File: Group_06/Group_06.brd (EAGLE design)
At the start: 100 x 80 mm, 29 parts, among them J1 POWER_JACKPTH_LOCK, U2 +12v

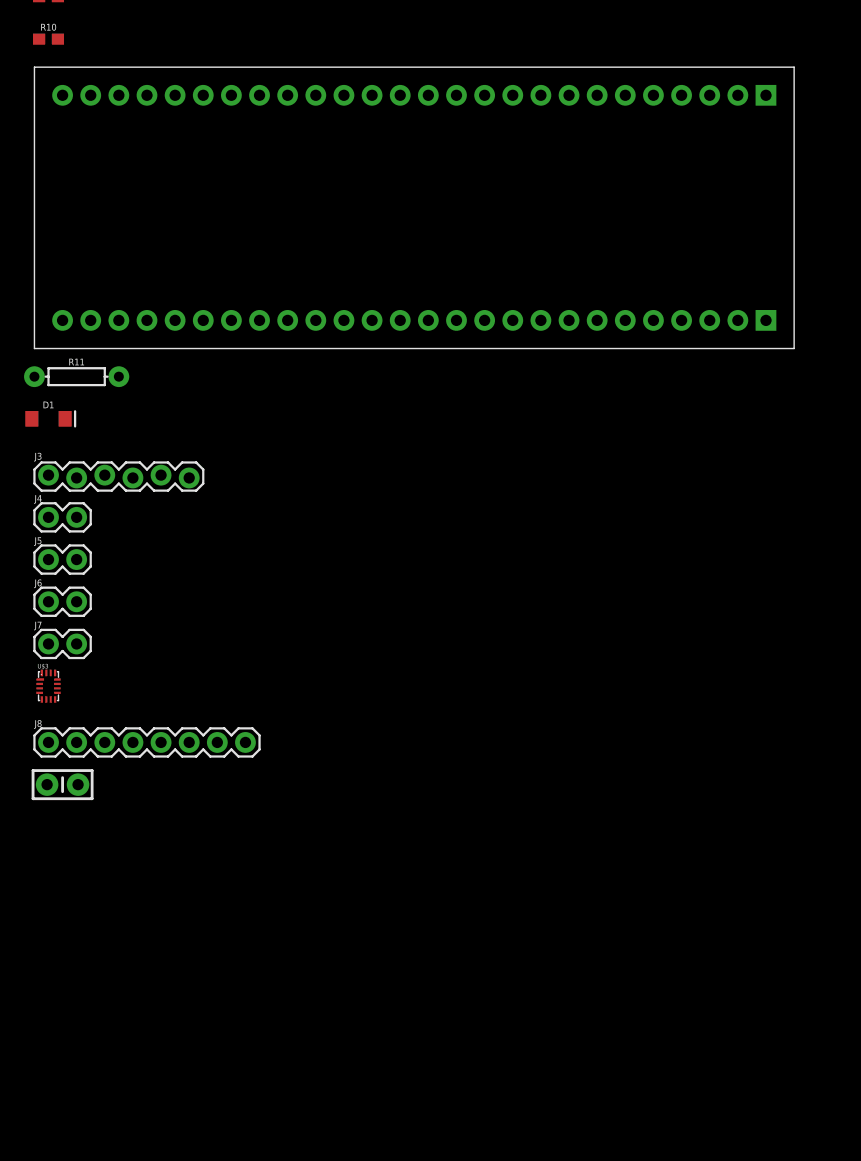
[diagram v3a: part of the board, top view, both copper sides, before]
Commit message: Change microcontroller and fixing connection problem
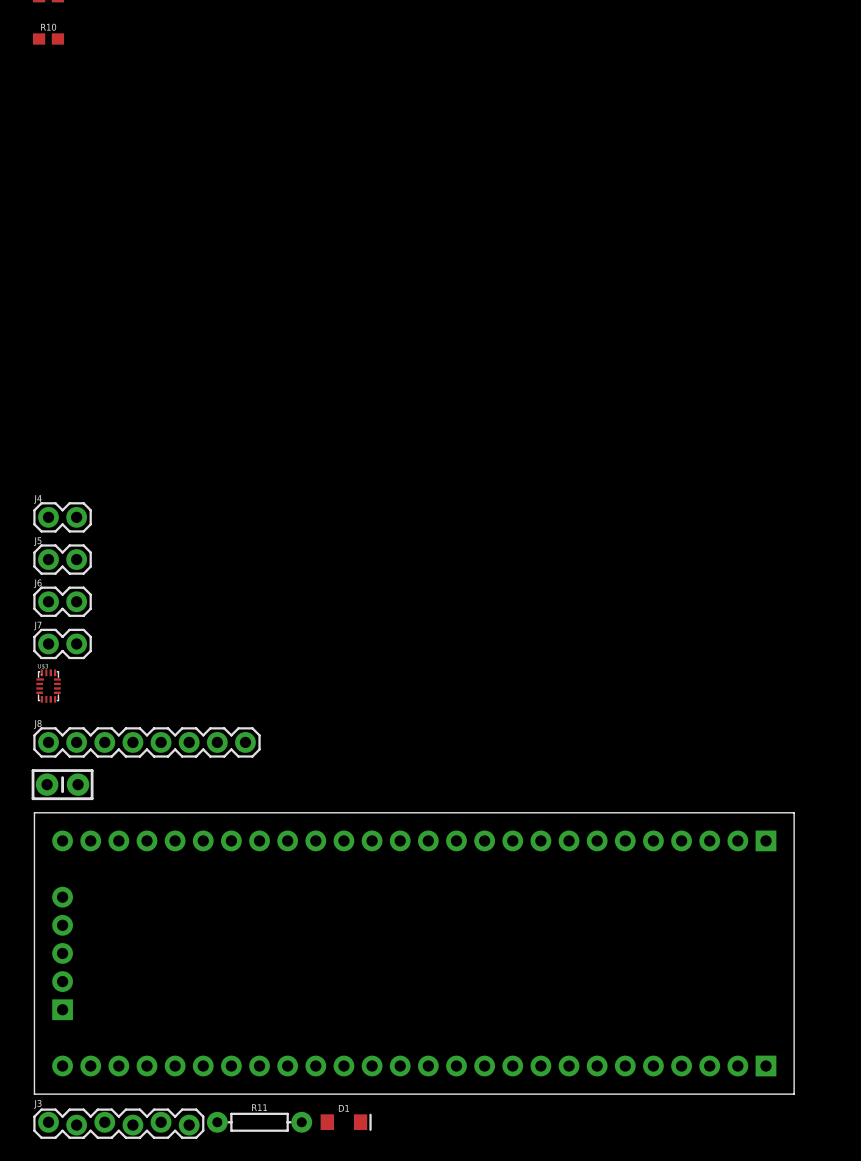
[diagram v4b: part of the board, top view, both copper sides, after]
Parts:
- U$2: value CY8CKIT-059_TARGET_3 -> CY8CKIT-059_TARGET; device CY8KIT-059:CY8CKIT-059_TARGET_3 -> CY8KIT-059:CY8CKIT-059_TARGET
- moved R11 69.3 mm to (-31.8, -143.5)
- moved D1 68.9 mm to (-24.1, -143.5)
- moved U$2 67.3 mm to (-16.5, -127.0)
- moved J3 58.4 mm to (-50.8, -143.5)
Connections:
- removed net GND2: U$2.52
- removed net MUX_A0/1.3C: U$3.15
- removed net MUX_A0/2.3C: U$2.24
- removed net MUX_A1/2.3C: U$2.23
- removed net MUX_A2/2.3C: U$2.22
- removed net MUX_OUT/2.5C: U$2.21
- removed net N$19: U$3.14
- removed net N$20: U$3.13
- removed net N$23: U$3.6
- new net MUX_A0: U$2.24, U$3.15
- new net MUX_A1: U$2.23, U$3.14
- new net MUX_A2: U$2.22, U$3.13
- new net MUX_OUT: U$2.21, U$3.6

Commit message: first try board
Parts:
- moved C3 226.3 mm to (95.2, 61.0), turned to 90 degrees
- moved J8 224.7 mm to (72.4, 78.7), turned to 180 degrees
- moved U$3 192.0 mm to (53.3, 57.1)
- moved J3 180.1 mm to (54.6, 2.54), turned to 180 degrees
- moved U$2 172.3 mm to (36.8, 36.8)
- moved J4 168.7 mm to (2.54, 71.1), turned to 90 degrees
- moved J5 166.3 mm to (2.54, 64.8), turned to 90 degrees
- moved J6 163.9 mm to (2.54, 58.4), turned to 90 degrees
- moved J7 161.5 mm to (2.54, 52.1), turned to 90 degrees
- moved R11 155.1 mm to (20.3, 2.54), turned to 180 degrees
- moved D1 149.5 mm to (7.62, 2.54)
- moved S1 148.0 mm to (80.0, 77.5), turned to 270 degrees
- moved U2 146.9 mm to (90.2, 73.7)
- moved C2 128.9 mm to (82.5, 61.0), turned to 90 degrees
- moved R10 119.4 mm to (14.0, 54.6), turned to 270 degrees
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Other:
- board size 100 x 80 mm -> 97.8 x 83.8 mm

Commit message: Board Layout 1
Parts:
- moved S1 72.0 mm to (55.0, 9.91), turned to 0 degrees
- moved U2 63.8 mm to (62.9, 16.0)
- moved C3 62.1 mm to (62.7, 8.00), turned to 180 degrees
- moved C2 60.0 mm to (62.7, 4.32), turned to 180 degrees
- moved J7 57.3 mm to (58.4, 64.8), turned to 180 degrees
- moved J1 55.9 mm to (47.6, 18.5), turned to 180 degrees
- moved J8 52.7 mm to (21.6, 64.8)
- moved J6 47.4 mm to (49.5, 64.8), turned to 180 degrees
- moved R10 44.9 mm to (58.4, 61.0)
- moved R9 44.9 mm to (55.9, 61.0)
- moved R8 43.6 mm to (49.5, 61.0)
- moved U$3 40.7 mm to (12.7, 55.9)
- moved J2 40.6 mm to (69.8, 7.62)
- moved R7 38.6 mm to (47.0, 61.0)
- moved J4 36.1 mm to (38.1, 64.8), turned to 0 degrees
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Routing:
- added copper zone on layer 16, net 5V
- added copper zone on layer 1, net GND
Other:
- board size 97.8 x 83.8 mm -> 72.4 x 69.8 mm

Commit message: Board Layout 2
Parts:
- moved J2 45.7 mm to (68.6, 53.3)
- moved J4 27.9 mm to (66.0, 64.8), turned to 180 degrees
- moved R4 27.9 mm to (66.0, 61.0)
- moved J7 26.7 mm to (31.8, 64.8)
- moved R10 26.7 mm to (31.8, 61.0)
- moved R9 26.7 mm to (29.2, 61.0)
- moved J5 26.7 mm to (54.6, 64.8), turned to 180 degrees
- moved R6 26.7 mm to (54.6, 61.0)
- moved R3 22.9 mm to (63.5, 61.0)
- moved R5 21.6 mm to (52.1, 61.0)
- moved R2 19.4 mm to (10.2, 20.8), turned to 0 degrees
- moved U2 19.2 mm to (43.7, 16.8), turned to 90 degrees
- moved C2 14.0 mm to (48.8, 5.59)
- moved C3 14.0 mm to (48.8, 9.27)
- moved S1 12.9 mm to (63.8, 19.4), turned to 90 degrees
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
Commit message: Board Layout 3
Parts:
- moved C3 27.1 mm to (22.1, 4.19)
- moved U2 9.67 mm to (35.3, 11.9), turned to 180 degrees
- moved R2 9.43 mm to (10.9, 11.4), turned to 90 degrees
- moved U1 8.03 mm to (26.7, 11.4), turned to 90 degrees
- moved D1 7.87 mm to (6.35, 10.8)
- moved R1 6.90 mm to (17.9, 12.1), turned to 0 degrees
- moved R11 6.52 mm to (10.0, 3.94), turned to 180 degrees
- moved C1 6.35 mm to (48.0, 14.7)
- moved J2 5.08 mm to (68.6, 48.3)
- moved U$3 5.08 mm to (12.7, 50.8)
- moved J4 5.08 mm to (66.0, 59.7)
- moved J5 5.08 mm to (54.6, 59.7)
- moved J6 5.08 mm to (43.2, 59.7)
- moved J7 5.08 mm to (31.8, 59.7)
- moved J8 5.08 mm to (21.6, 59.7)
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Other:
- board size 72.4 x 69.8 mm -> 72.4 x 63.5 mm
